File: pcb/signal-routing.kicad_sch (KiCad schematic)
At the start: 42 parts, among them U10 SN74LVC1G3157DCKR, U11 SN74HCS595PWR, U3 SN74LVC1G3157DCKR, U4 SN74LVC1G3157DCKR, U5 SN74LVC1G3157DCKR, U6 SN74LVC1G3157DCKR, U7 SN74LVC1G3157DCKR, U8 SN74LVC1G3157DCKR, U9 SN74LVC1G3157DCKR

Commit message: 1st step OEPSPN & MPN on components
- still missing new codes to be emitted
- project/schematic/components not tunned with Jon's project at this date
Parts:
- C16, C17, C18, C19, C20, C21, C22, C23, C24, C25, C26, C27, C28, C29, C30, C31: MPN (none) -> GRM155R71E103KA01D; OEPSPN (none) -> OEPS010067
- C32: value 0.1uF -> 100nF; MPN (none) -> C1005X7R1E104K050BB; OEPSPN (none) -> OEPS010050
- R10, R11, R12, R13, R18, R19, R20, R21: MPN (none) -> RG1005P-104-B-T5; OEPSPN (none) -> OEPS020175
- R14, R15, R16, R17, R6, R7, R8, R9: value 200 -> 200R; MPN (none) -> ERA-2AEB201X; OEPSPN (none) -> OEPS020171
- U10, U3, U4, U5, U6, U7, U8, U9: MPN (none) -> SN74LVC1G3157DCKR; OEPSPN (none) -> espera
- U11: MPN (none) -> SN74HCS595PWR; OEPSPN (none) -> espera

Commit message: all OEPSPN
- all components with OEPSPN completed
- this Project Fork version not tunned with Project Main Branch
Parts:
- U10, U3, U4, U5, U6, U7, U8, U9: OEPSPN espera -> OEPS080161
- U11: OEPSPN espera -> OEPS080159
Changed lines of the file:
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@@
 			)
 		)
-		(property "OEPSPN" "espera"
+		(property "OEPSPN" "OEPS080161"
 			(at 152.4 127 0)
 			(effects
@@
 			)
 		)
-		(property "OEPSPN" "espera"
+		(property "OEPSPN" "OEPS080159"
 			(at 215.9 90.17 0)
 			(effects
@@
 			)
 		)
-		(property "OEPSPN" "espera"
+		(property "OEPSPN" "OEPS080161"
 			(at 77.47 127 0)
 			(effects
@@
 			)
 		)
-		(property "OEPSPN" "espera"
+		(property "OEPSPN" "OEPS080161"
 			(at 77.47 82.55 0)
 			(effects
@@
 			)
 		)
-		(property "OEPSPN" "espera"
+		(property "OEPSPN" "OEPS080161"
 			(at 152.4 171.45 0)
 			(effects
@@
 			)
 		)
-		(property "OEPSPN" "espera"
+		(property "OEPSPN" "OEPS080161"
 			(at 77.47 171.45 0)
 			(effects
@@
 			)
 		)
-		(property "OEPSPN" "espera"
+		(property "OEPSPN" "OEPS080161"
 			(at 152.4 82.55 0)
 			(effects
@@
 			)
 		)
-		(property "OEPSPN" "espera"
+		(property "OEPSPN" "OEPS080161"
 			(at 77.47 38.1 0)
 			(effects
@@
 			)
 		)
-		(property "OEPSPN" "espera"
+		(property "OEPSPN" "OEPS080161"
 			(at 152.4 38.1 0)
 			(effects

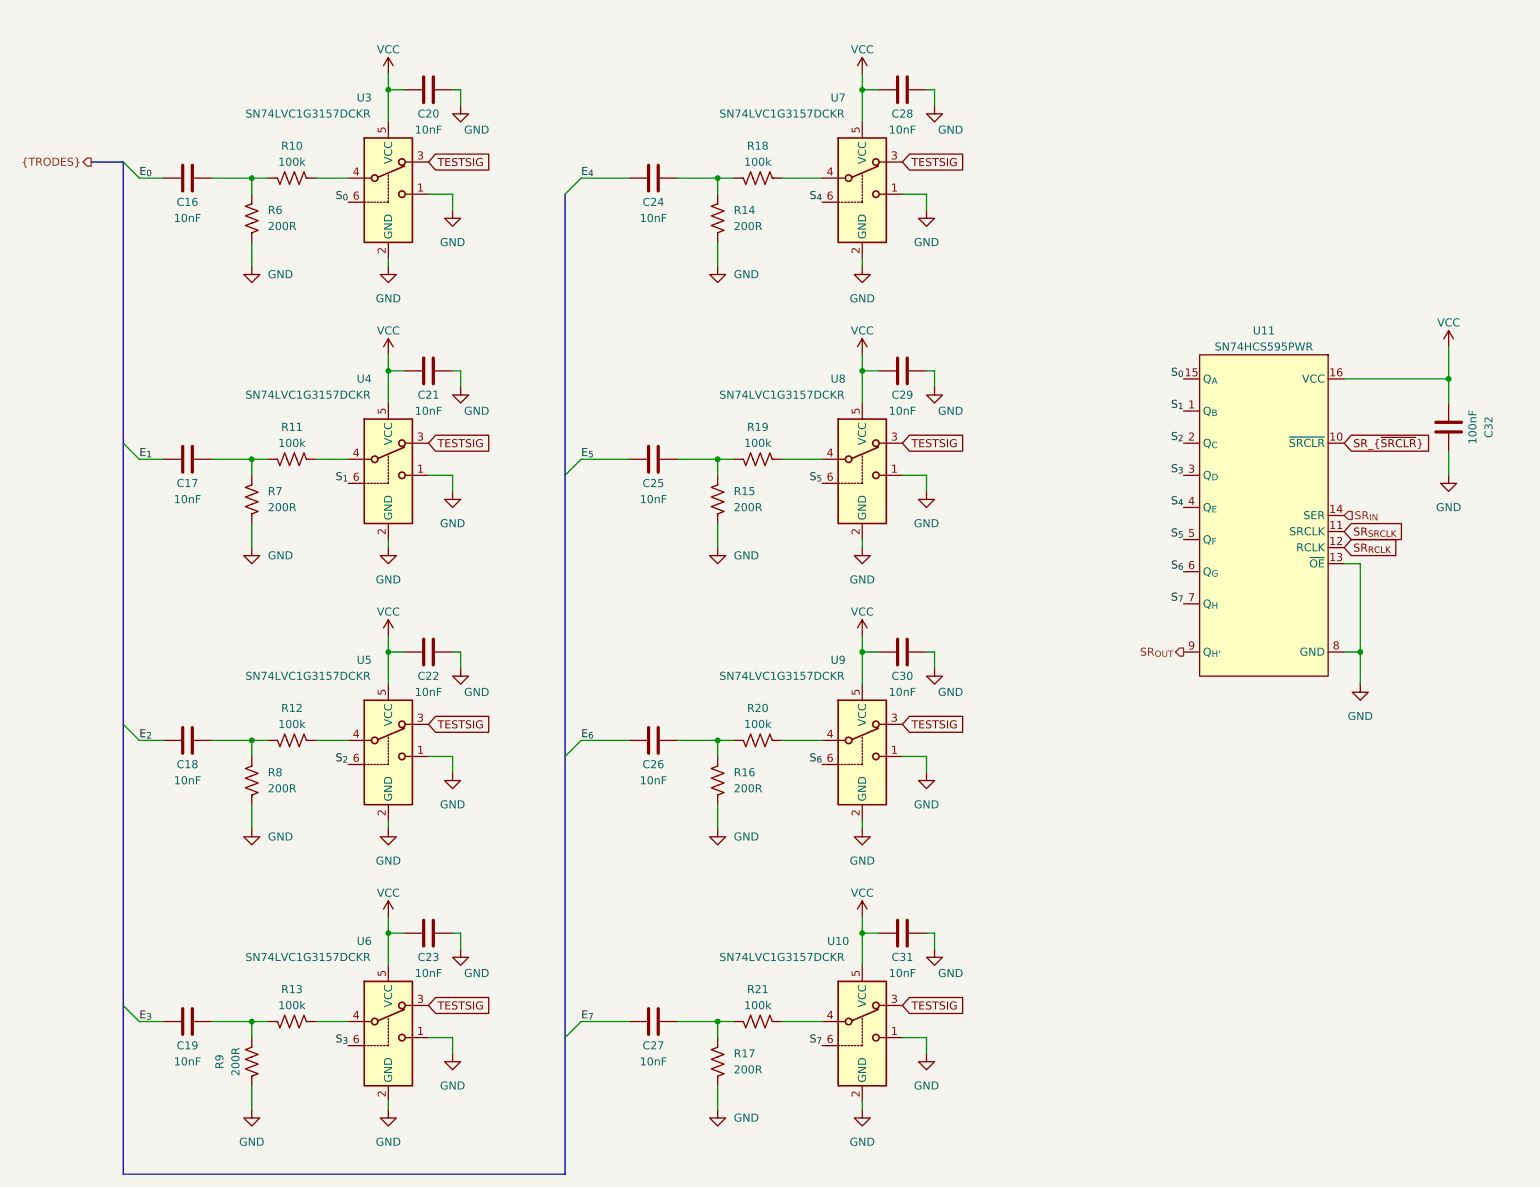
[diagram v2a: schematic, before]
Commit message: tunned with Main branch
- OEPSPN & MPN already on components
- missing 4 these codes
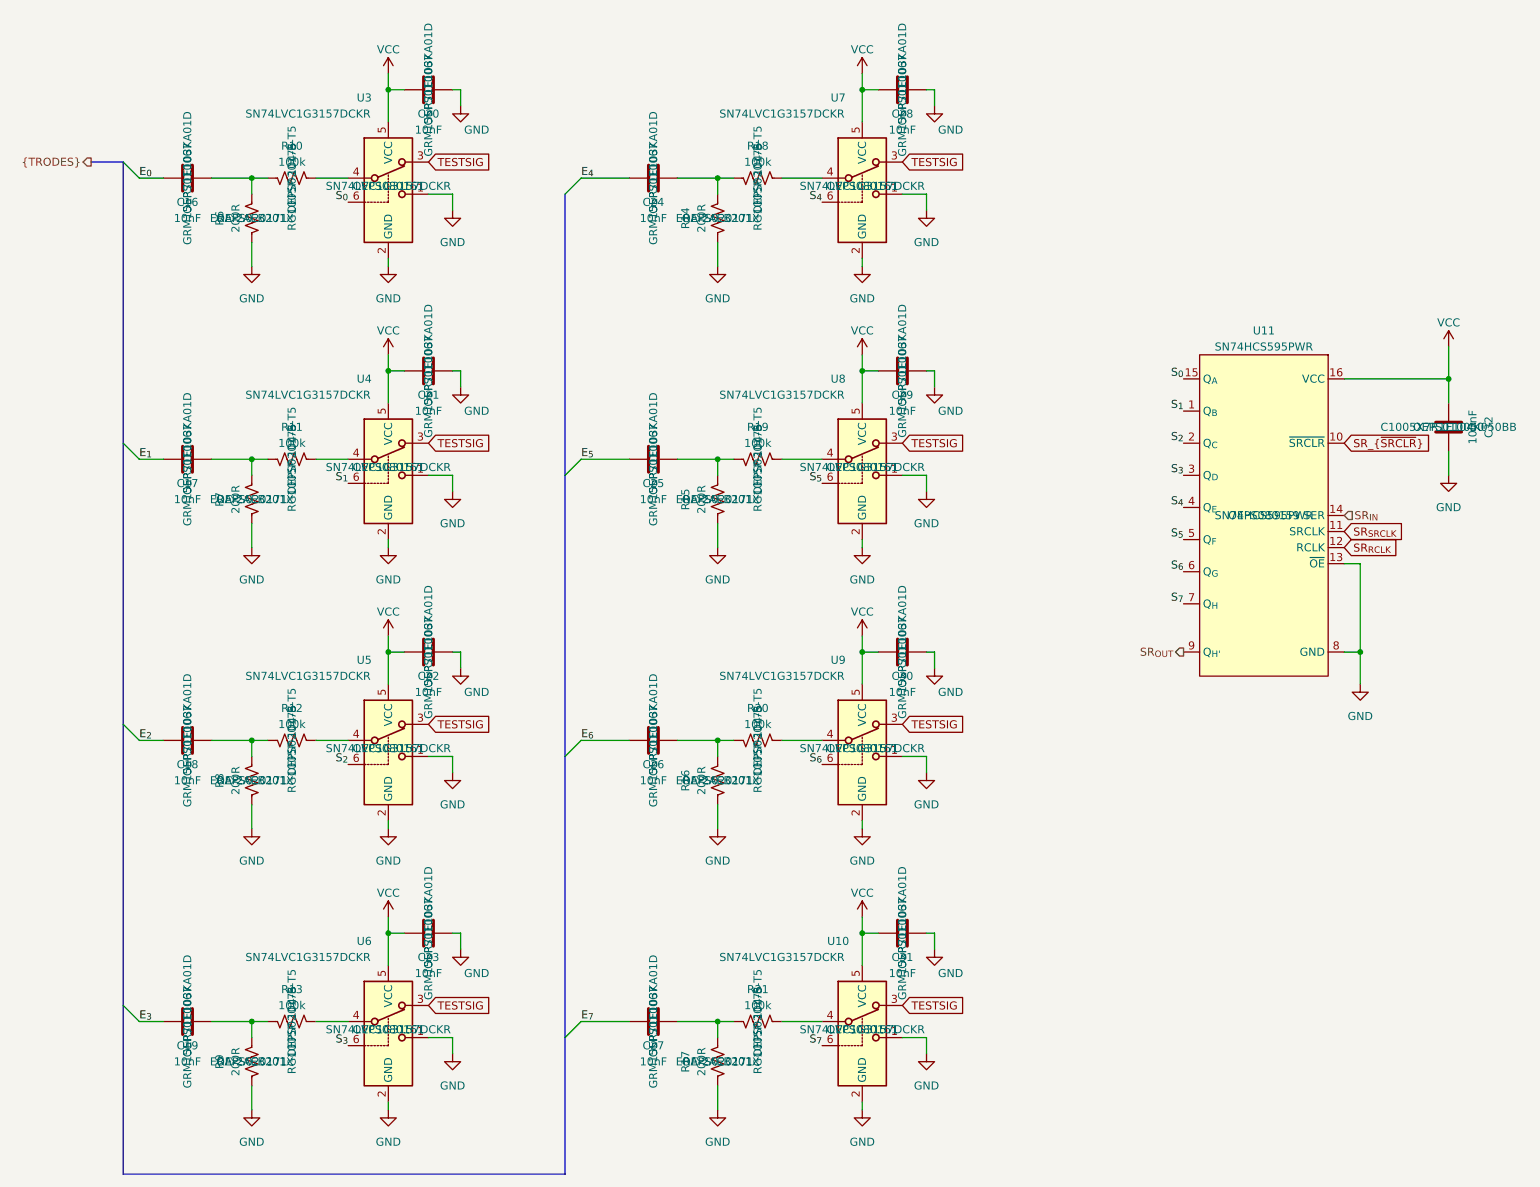
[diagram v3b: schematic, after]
